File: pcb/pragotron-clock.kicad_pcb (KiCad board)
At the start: 2 copper layers, 44 x 61 mm, 20 parts, among them J1 Conn_01x02, J2 Conn_01x03, J3 Conn_01x03, J6 Conn_01x04, J7 694108301002, U1 L293D

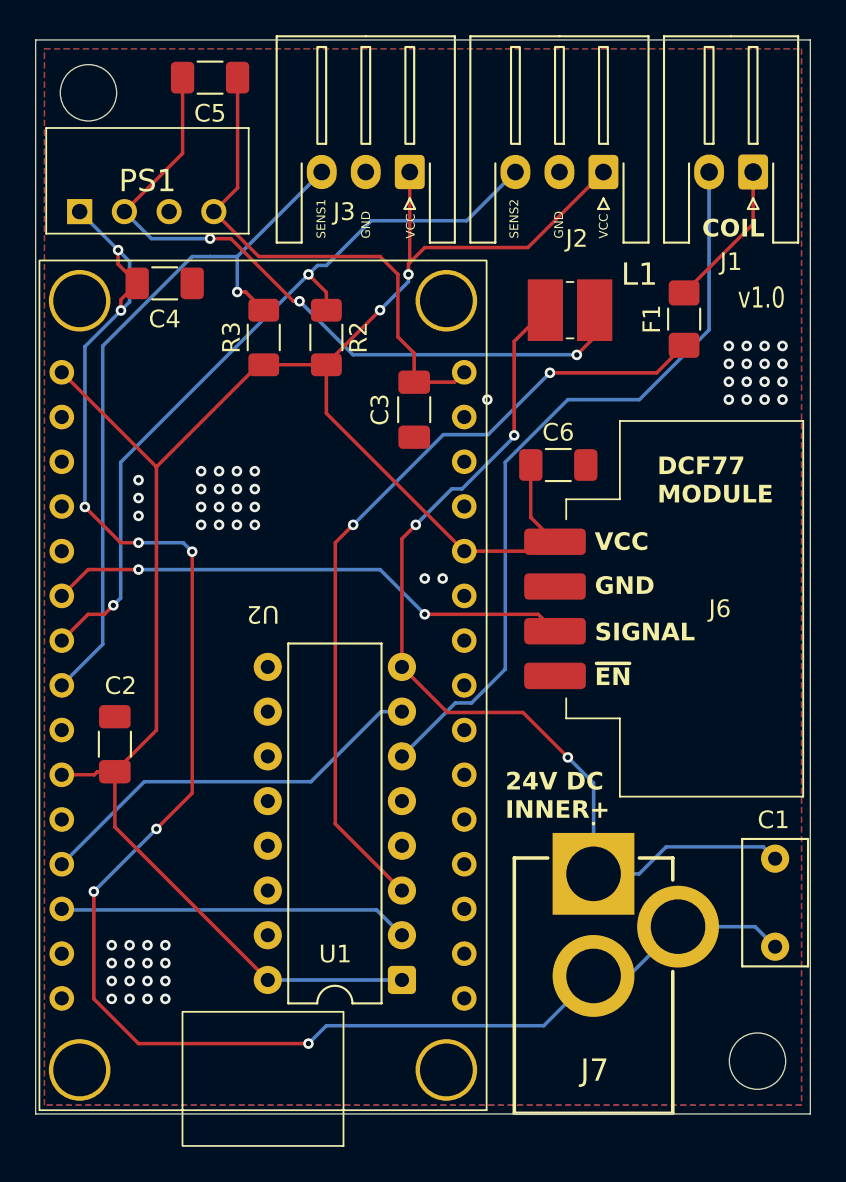
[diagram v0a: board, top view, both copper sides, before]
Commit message: remove ground separation, turn around esp8266
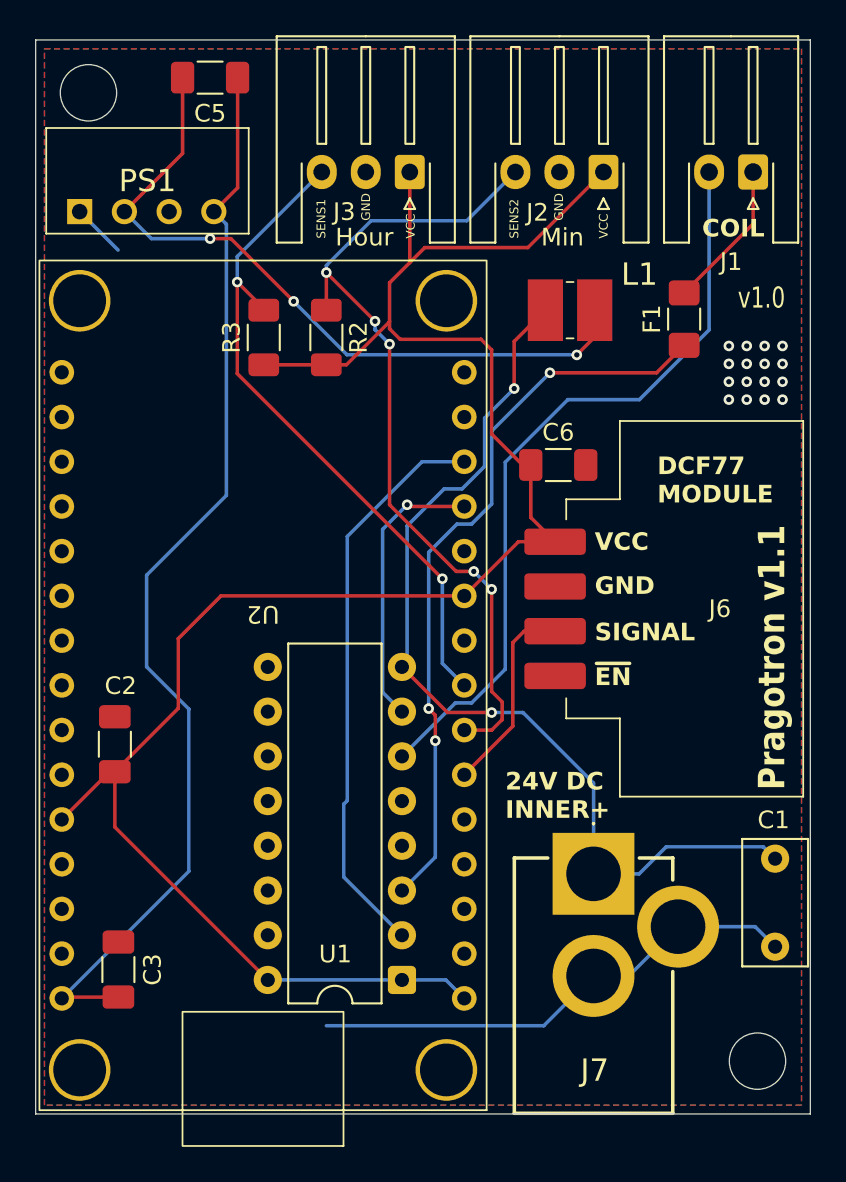
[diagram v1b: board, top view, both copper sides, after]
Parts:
- removed C4: 300p, Capacitor_SMD:C_1206_3216Metric_Pad1.33x1.80mm_HandSolder
- F1: value Fuse -> 200mA T
- moved C3 36.0 mm to (84.2, 154.8), turned to 90 degrees
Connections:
- C1 pad 2: /VIN- -> GND
- J7 pad 2: /VIN- -> GND
- J7 pad 3: /VIN- -> GND
- PS1 pad 1: /VIN- -> GND
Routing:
- net /VIN-: track 101.1 -> 0.00 mm, vias 8 -> 0
- net +5V: track 29.7 -> 61.5 mm
- net GND: track 0.00 -> 31.4 mm, vias 54 -> 16
- net /DCF_SIG: track 30.1 -> 11.3 mm, vias 2 -> 0
- net /OUT1_POSITIVE: track 19.9 -> 32.5 mm
- net /OUT1_NEGATIVE: track 22.9 -> 16.1 mm, vias 0 -> 1
- net /SENS2: track 43.8 -> 48.0 mm, vias 2 -> 5
- net Net-(U1-1Y): track 45.8 -> 42.0 mm, vias 2 -> 3
- net /SENS1: track 40.7 -> 38.7 mm, vias 1 -> 2
- net +24V: track 54.0 -> 54.2 mm, vias 3 -> 2
- net +3V3: vias 2 -> 0
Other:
- board text added: "Hour"
- board text added: "Min"
- board text added: "Pragotron v1.1"
